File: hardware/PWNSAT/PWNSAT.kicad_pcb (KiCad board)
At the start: 2 copper layers, 83 x 83 mm, 116 parts, among them J1 Conn_01x03, J2 Conn_01x04_Pin, J3 Sensors, J4 USB_A, J5 USB_A, J6 Source, SW1 SW_Push, SW2 SW_Push, SW4 USB Selector, U2 W25N02KVZEIR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

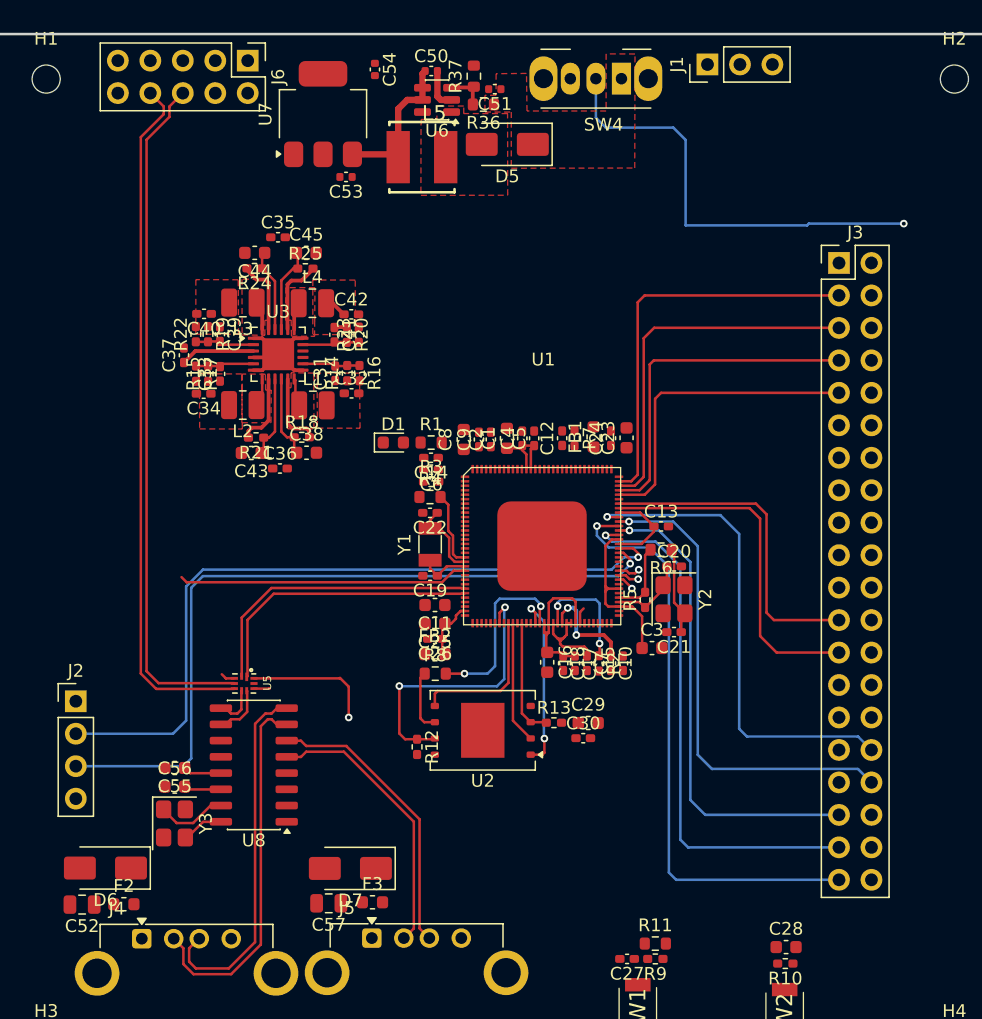
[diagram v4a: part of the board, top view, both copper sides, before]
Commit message: feat(Hw):Route_Updating_PWNCube_Board
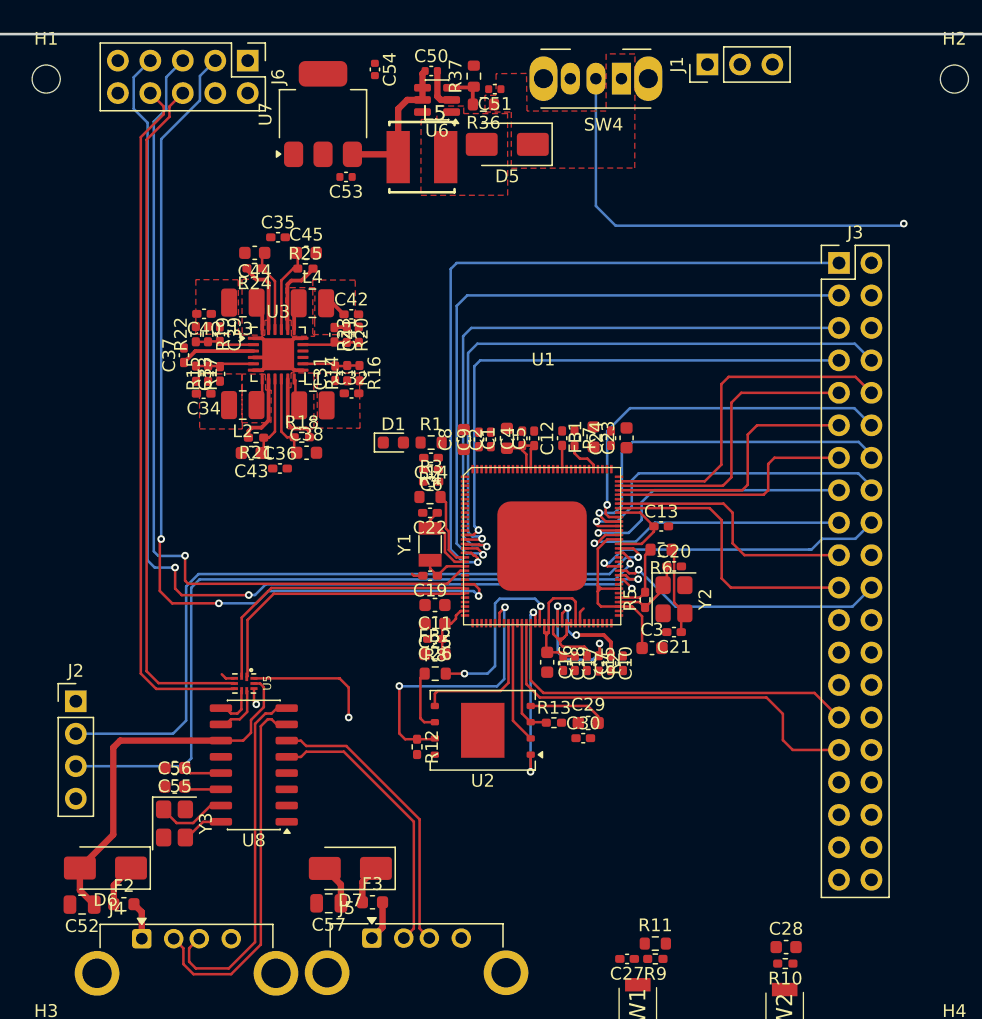
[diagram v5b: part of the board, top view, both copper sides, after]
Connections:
- J3 pad 1: /Sensor/DIO2 -> /Sensor/R0_BUSY
- J3 pad 10: /Sensor/SCL_ICM -> /Sensor/R0_NSS
- J3 pad 11: /Sensor/R0_RST -> /Sensor/R0_MOSI
- J3 pad 12: /Sensor/AP_ADO -> /Sensor/R1_DIO1
- J3 pad 13: /Sensor/R0_BUSY -> /Sensor/R0_MISO
- J3 pad 14: /Sensor/INT1 -> /Sensor/R1_DIO2
- J3 pad 15: /Sensor/R0_DIO3 -> /Sensor/R1_BUSY
- J3 pad 16: /Sensor/FSYNC -> /Sensor/R1_DIO3
- J3 pad 17: /Sensor/R0_DIO2 -> /Sensor/R1_RST
- J3 pad 18: /Sensor/INT2 -> /Sensor/SDA_BME280
- J3 pad 19: /Sensor/R0_DIO1 -> /Sensor/R1_ANT_SW
- J3 pad 20: /Sensor/SDA_BME280 -> /Sensor/SDA_ICM
- J3 pad 21: /Sensor/R0_ANT_SW -> /Sensor/DIO23
- J3 pad 22: /Sensor/SCL_BME280 -> /Sensor/SCL_ICM
- J3 pad 23: /Sensor/R1_ANT_SW -> /Sensor/R0_ANT_SW
- J3 pad 25: /Sensor/DIO23 -> /Sensor/R1_NSS
- J3 pad 27: /Sensor/R1_NSS -> /Sensor/R1_SCK
- J3 pad 29: /Sensor/R1_SCK -> /Sensor/R1_MOSI
- J3 pad 3: /Sensor/R0_NSS -> /Sensor/R0_RST
- J3 pad 32: /Sensor/R1_DIO1 -> /Sensor/FSYNC
- J3 pad 33: /Sensor/R1_MOSI -> /Sensor/SCL_BME280
- J3 pad 34: /Sensor/R1_DIO2 -> /Sensor/INT1
- J3 pad 35: /Sensor/R1_BUSY -> /Sensor/AP_ADO
- J3 pad 37: /Sensor/R1_RST -> /Sensor/DIO2
- J3 pad 39: /Sensor/R1_DIO3 -> /Sensor/INT2
- J3 pad 5: /Sensor/R0_SCK -> /Sensor/R0_DIO3
- J3 pad 7: /Sensor/R0_MOSI -> /Sensor/R0_DIO1
- J3 pad 8: /Sensor/SDA_ICM -> /Sensor/R0_DIO2
- J3 pad 9: /Sensor/R0_MISO -> /Sensor/R0_SCK
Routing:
- net /Source_Connector/Enable: track 1.63 -> 82.7 mm, vias 1 -> 3
- net /Source_Connector/USB_DET: track 0.00 -> 71.0 mm, vias 0 -> 3
- net /Sensor/R0_BUSY: track 0.00 -> 56.5 mm, vias 0 -> 1
- net /Sensor/R0_RST: track 0.00 -> 52.9 mm, vias 0 -> 1
- net /Sensor/R0_DIO3: track 0.00 -> 49.3 mm, vias 0 -> 1
- net /Sensor/R0_DIO2: track 0.00 -> 49.1 mm, vias 0 -> 1
- net /Source_Connector/Battery: track 22.7 -> 66.3 mm, vias 0 -> 1
- net /Sensor/R0_DIO1: track 0.00 -> 42.9 mm, vias 0 -> 1
- net +5V: track 0.00 -> 33.2 mm
- net /Sensor/R1_MOSI: track 0.00 -> 32.6 mm
- net /Sensor/R1_MISO: track 0.00 -> 29.8 mm
- net /Sensor/SDA_BME280: track 0.00 -> 23.5 mm, vias 0 -> 1
- net /Sensor/SCL_BME280: track 1.74 -> 21.8 mm
- net /Sensor/R1_RST: track 42.0 -> 22.0 mm
- net /Sensor/R1_DIO3: track 46.6 -> 27.0 mm
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
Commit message: feat(Hw):Route_UpdatedPWNcube_
Pending_3v3
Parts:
- moved C54 10.8 mm to (45.2, 29.3), turned to 180 degrees
- moved J6 2.56 mm to (41.8, 22.8)
- moved C14 1.89 mm to (56.1, 53.2)
- moved R3 0.95 mm to (56.2, 52.2)
- moved C6 0.94 mm to (56.2, 51.3)
- moved C30 0.75 mm to (68.6, 73.9), turned to 180 degrees
- moved C29 0.69 mm to (68.6, 72.7)
- moved C16 0.69 mm to (65.1, 67.8)
- moved C22 0.65 mm to (55.6, 55.5)
- moved Y1 0.65 mm to (55.6, 58.0)
- moved C19 0.60 mm to (55.7, 60.5)
- moved C15 0.59 mm to (70.9, 67.7), turned to -90 degrees
- moved C10 0.57 mm to (70.0, 67.7)
- moved C18 0.57 mm to (66.3, 67.7)
- moved C7 0.55 mm to (68.1, 67.7)
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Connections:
- J3 pad 20: /Sensor/SDA_ICM -> /Sensor/SCL_BME280
- J3 pad 22: /Sensor/SCL_ICM -> /Sensor/SDA_ICM
- J3 pad 23: /Sensor/R0_ANT_SW -> /Sensor/SCL_ICM
- J3 pad 25: /Sensor/R1_NSS -> /Sensor/AP_ADO
- J3 pad 27: /Sensor/R1_SCK -> /Sensor/DIO2
- J3 pad 29: /Sensor/R1_MOSI -> /Sensor/R0_ANT_SW
- J3 pad 33: /Sensor/SCL_BME280 -> /Sensor/R1_MOSI
- J3 pad 35: /Sensor/AP_ADO -> /Sensor/INT2
- J3 pad 37: /Sensor/DIO2 -> /Sensor/R1_NSS
- J3 pad 39: /Sensor/INT2 -> /Sensor/R1_SCK
- SW4 pad 1: +5V -> GND
- SW4 pad 3: GND -> +5V
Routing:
- net +3V3: track 8.57 -> 229.7 mm, vias 0 -> 5
- net +1V8: track 7.98 -> 152.6 mm, vias 2 -> 12
- net +5V: track 33.2 -> 166.6 mm, vias 0 -> 15
- net VCC: track 41.3 -> 130.6 mm, vias 0 -> 3
- net /core/VCC_DDR: track 14.4 -> 98.6 mm, vias 0 -> 4
- net /core/VDD_ARM: track 28.0 -> 108.9 mm, vias 0 -> 8
- net +3.3V: track 0.00 -> 79.4 mm, vias 0 -> 3
- net GND: track 25.8 -> 91.8 mm, vias 1 -> 50
- net /Sensor/R1_NSS: track 0.00 -> 51.9 mm, vias 0 -> 1
- net /core/NPOR: track 0.00 -> 49.1 mm, vias 0 -> 2
- net /core/RECOVERY: track 0.00 -> 48.3 mm, vias 0 -> 2
- net /Sensor/R1_SCK: track 0.00 -> 47.9 mm, vias 0 -> 1
- net /core/GPIO: track 0.00 -> 45.7 mm
- net /Sensor/INT2: track 0.00 -> 37.4 mm, vias 0 -> 1
- net /USB_Selector/S: track 44.8 -> 82.1 mm, vias 2 -> 3
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- added copper zone on B.Cu, net +5V
- added copper zone on F.Cu, net VCC

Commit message: feat(Hw):Update_Route_And_3d_Model_PWNsat_Batt_Board_And_Sensors
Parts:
- moved SW4 5.52 mm to (76.8, 21.0)
- moved C50 5.52 mm to (61.9, 20.4)
- moved C53 5.52 mm to (55.2, 28.7)
- moved C54 5.52 mm to (50.7, 28.6)
- moved D5 5.52 mm to (67.8, 26.1)
- moved C51 5.52 mm to (66.8, 21.8)
- moved J1 5.52 mm to (83.5, 19.9)
- moved R36 5.52 mm to (66.0, 23.0)
- moved R37 5.52 mm to (65.2, 20.8)
- moved U6 5.52 mm to (62.3, 22.7)
- moved U7 5.52 mm to (53.4, 23.8)
- moved L5 5.44 mm to (61.1, 27.5)
- moved J6 3.06 mm to (44.1, 20.7)
- moved R10 0.61 mm to (83.5, 90.9)
- moved C28 0.29 mm to (83.9, 89.6)
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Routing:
- net VCC: track 130.6 -> 110.2 mm, vias 3 -> 6
- net /Sensor/R1_NSS: track 51.9 -> 43.4 mm
- net /core/NPOR: track 49.1 -> 56.6 mm
- net /USB_Selector/S: track 82.1 -> 87.9 mm
- net +5V: track 166.6 -> 172.2 mm
- net +3V3: track 229.7 -> 235.2 mm, vias 5 -> 6
- net /core/GPIO: track 45.7 -> 51.0 mm
- net /Source_Connector/2_DP: track 50.9 -> 55.8 mm
- net /Source_Connector/USB_DET: track 69.9 -> 74.1 mm
- net /Source_Connector/2_DN: track 52.0 -> 55.1 mm
- net /Source_Connector/Battery: track 66.0 -> 68.9 mm
- net +1V8: track 152.6 -> 150.1 mm
- net /core/FSPI_CS0N: track 14.3 -> 16.5 mm
- net +3.3V: track 79.4 -> 81.5 mm
- net /Source_Connector/Enable: track 92.5 -> 94.3 mm
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
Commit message: feat(Hw):Boards_Updated
Pending_Sensors_Board
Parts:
- removed J1: Conn_01x03, Connector_PinHeader_2.54mm:PinHeader_1x03_P2.54mm_Vertical
- added R26: 4.7K, Resistor_SMD:R_0402_1005Metric_Pad0.72x0.64mm_HandSolder, F.Cu at (30.8, 68.1)
- added R27: 4.7K, Resistor_SMD:R_0402_1005Metric_Pad0.72x0.64mm_HandSolder, F.Cu at (30.8, 72.1)
- J2: footprint Connector_PinHeader_2.54mm:PinHeader_1x04_P2.54mm_Vertical -> Connector_PinHeader_2.54mm:PinHeader_1x06_P2.54mm_Vertical
- moved SW4 76.0 mm to (69.3, 96.7), turned to 0 degrees
- moved SW1 69.5 mm to (81.7, 25.8), turned to -90 degrees
- moved C28 69.5 mm to (89.1, 20.3)
- moved SW2 69.5 mm to (89.3, 25.8)
- moved R10 69.5 mm to (88.7, 21.6)
- moved C27 61.4 mm to (82.5, 30.1), turned to 0 degrees
- moved R9 60.8 mm to (80.3, 30.1), turned to 0 degrees
- moved R11 58.4 mm to (80.3, 31.3), turned to 180 degrees
- moved D1 35.3 mm to (75.8, 22.8), turned to -90 degrees
- moved R1 31.2 mm to (75.8, 25.7), turned to -90 degrees
- moved J2 5.07 mm to (28.6, 65.3)
- moved C19 0.39 mm to (55.3, 60.5)
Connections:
- net /Sensor/SCL_BME280 renamed /Sensor/SCL_SENS
- net /Sensor/SDA_BME280 renamed /Sensor/SDA_SENS
- J2 pad 2: /core/DEBUG_RX -> /core/SCL
- J2 pad 3: /core/DEBUG_TX -> /core/SDA
- J2 pad 4: +3V3 -> /core/DEBUG_RX
- J3 pad 22: /Sensor/SDA_ICM -> unconnected-(J3-Pin_22-Pad22)
- J3 pad 23: /Sensor/SCL_ICM -> unconnected-(J3-Pin_23-Pad23)
- U1 pad 112: /core/GPIO -> unconnected-(U1D-SDMMC1_CMD_M0/I2S0_SDO3_SDI1/VO_LCDC_D11/GP_IO2_A3_D-Pad112)
- U1 pad 72: /Sensor/SCL_ICM -> /core/SCL
- U1 pad 73: /Sensor/SDA_ICM -> /core/SDA
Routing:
- net /core/SDA: track 0.00 -> 55.5 mm, vias 0 -> 2
- net /core/SCL: track 0.00 -> 52.9 mm, vias 0 -> 2
- net /core/GPIO: track 51.0 -> 0.00 mm
- net /core/LED: track 5.02 -> 48.5 mm, vias 0 -> 2
- net +5V: track 172.2 -> 209.8 mm
- net +1V8: track 150.1 -> 182.4 mm
- net /USB_Selector/S: track 87.9 -> 59.3 mm, vias 3 -> 2
- net /Sensor/SCL_ICM: track 21.6 -> 0.00 mm, vias 1 -> 0
- net /Sensor/SDA_ICM: track 21.1 -> 0.00 mm, vias 1 -> 0
- net /core/NPOR: track 56.6 -> 72.1 mm
- net /core/VDD_ARM: track 109.5 -> 101.5 mm
- net /core/RECOVERY: track 48.3 -> 55.9 mm
- net GND: track 93.4 -> 88.1 mm, vias 50 -> 47
- net +3V3: track 235.2 -> 239.6 mm, vias 6 -> 7
- net /core/FSPI_CS0N: track 16.5 -> 13.5 mm
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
